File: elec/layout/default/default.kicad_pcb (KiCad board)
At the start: 4 copper layers, 76 x 146 mm, 103 parts, among them J1 ?, J2 ?, Q1 ?, SW1 ?, SW10 ?, SW11 ?, SW12 ?, SW13 ?, SW14 ?, SW15 ?, SW16 ?, SW17 ?, SW18 ?, SW19 ?, SW2 ?, SW20 ?, SW21 ?, SW22 ?, SW23 ?, SW24 ?, SW25 ?, SW26 ?, SW27 ?, SW28 ?, SW29 ?, SW3 ?, SW30 ?, SW31 ?, SW32 ?, SW33 ?, SW34 ?, SW35 ?, SW36 ?, SW37 ?, SW38 ?, SW39 ?, SW4 ?, SW40 ?, SW5 ?, SW6 ?, SW7 ?, SW8 ?, SW9 ?, U1 ?, U2 ?, U3 ?, U4 ?, U5 ?, U6 ?, U7 ?, U8 ?

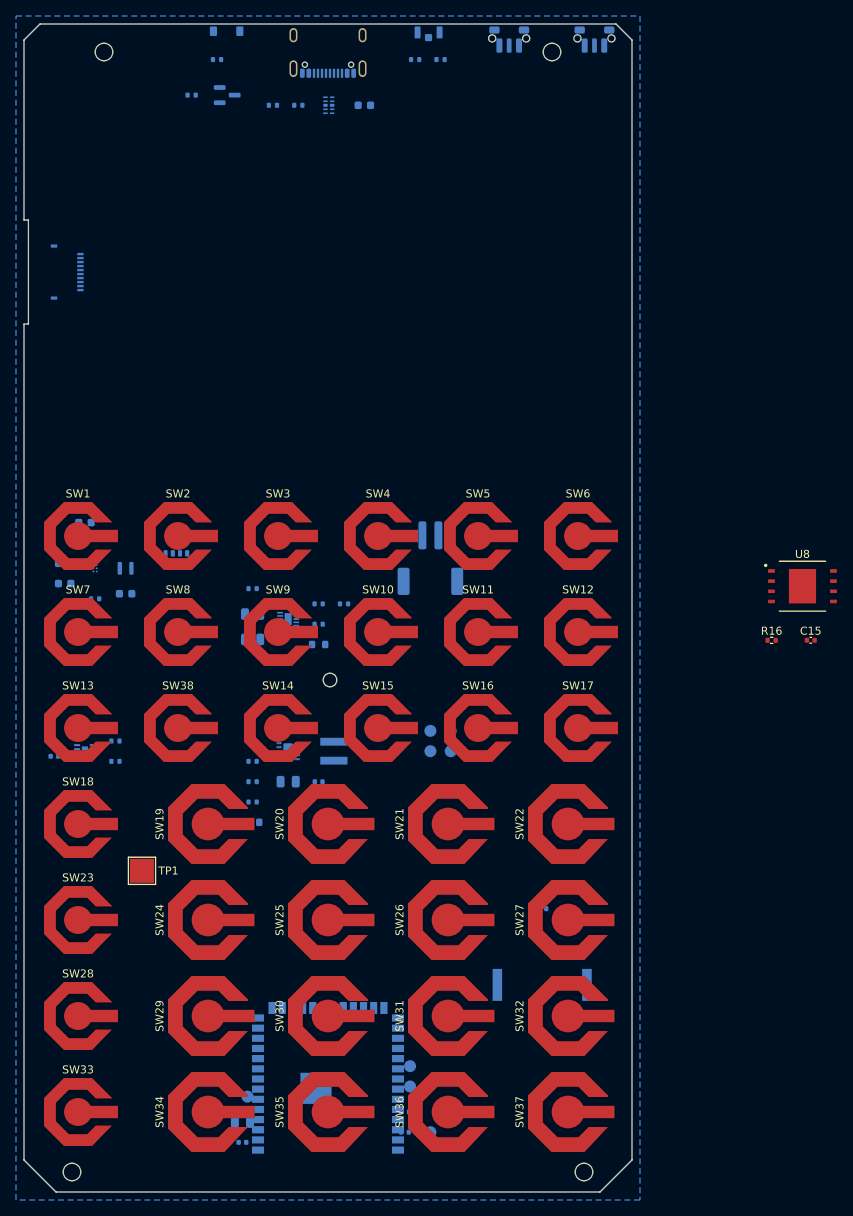
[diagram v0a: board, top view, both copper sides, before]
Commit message: mip: WROOM area and NAND placed, board fully rerouted at 146
104 nets, 0 failed; check_ends, check_pour, NPTH clean; antenna keepout
X 14..62 from Y 141.25 empty. fix_footprint_zones.py mirrors zones of
back-side footprints (U5's keepout; both Alps keepouts were on the wrong
side). C8/C9 share U5 pin 2's plane via. Bench pin map for the Waveshare
LCD-Driver board in docs/bench-lcd-driver-board.md.

Co-Authored-By: Claude Opus 5.5 (1M context) <noreply@anthropic.com>
Claude-Session: https://claude.ai/code/session_01Fsrot3PauY1JdFC7HgzJ33
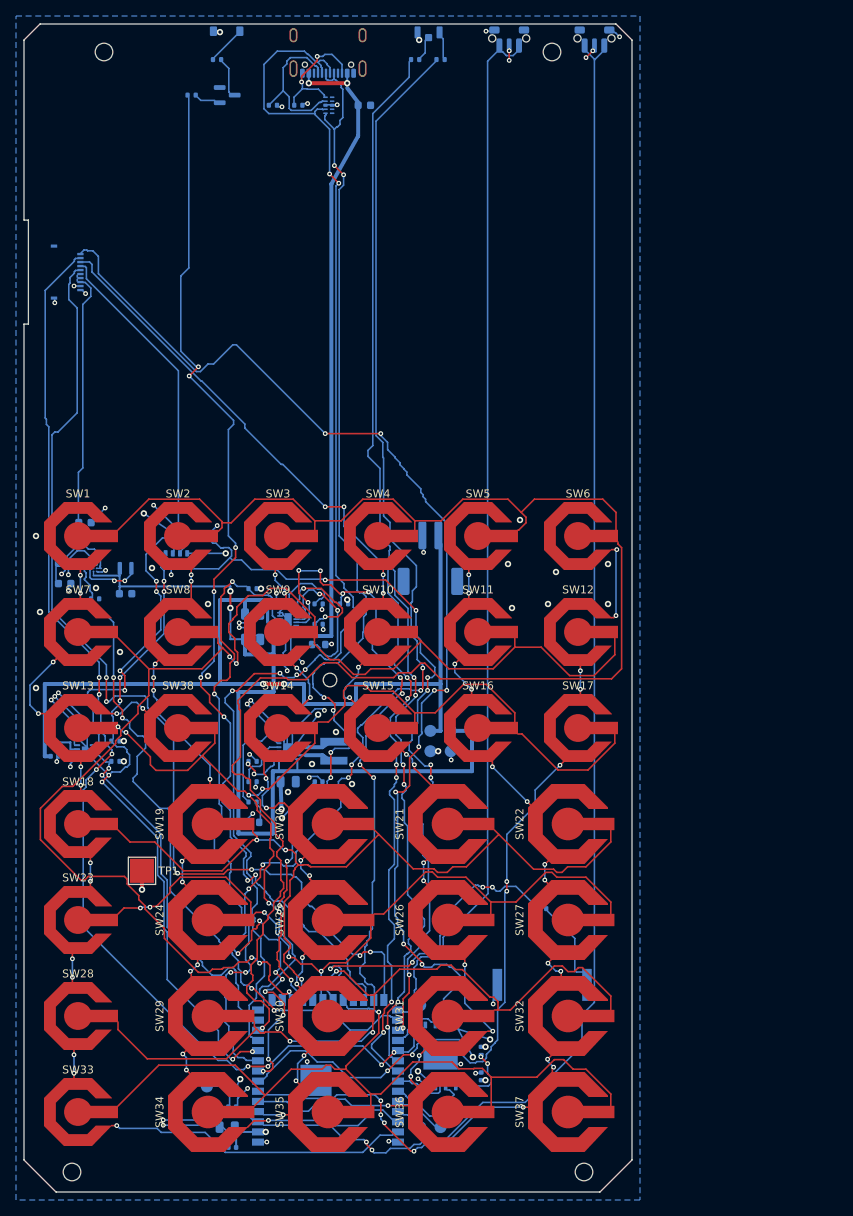
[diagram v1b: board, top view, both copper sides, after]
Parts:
- C15, R16, U8: moved to B.Cu
- moved U8 74.1 mm to (52.1, 129.0), turned to 90 degrees
- moved C15 68.3 mm to (57.1, 131.5), turned to 90 degrees
- moved R16 62.9 mm to (57.1, 128.4), turned to 90 degrees
- moved TP8 28.5 mm to (22.9, 132.8)
- moved TP9 24.4 mm to (49.5, 122.7)
- moved C7 21.8 mm to (26.0, 135.3)
- moved R13 21.8 mm to (26.0, 132.8)
- moved TP7 8.52 mm to (52.1, 137.9)
- moved TP6 5.24 mm to (49.5, 137.9)
- moved C8 2.01 mm to (25.4, 137.9), turned to 180 degrees
- moved C9 1.42 mm to (26.0, 140.4), turned to 180 degrees
- moved U5 1.00 mm to (38.0, 134.5)
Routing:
- net row0: track 0.00 -> 200.1 mm, vias 0 -> 1
- net en: track 0.00 -> 180.6 mm, vias 0 -> 2
- net row1: track 0.00 -> 164.0 mm, vias 0 -> 5
- net usb_dm: track 0.00 -> 157.1 mm, vias 0 -> 6
- net led_red: track 0.00 -> 151.9 mm, vias 0 -> 8
- net mip_sck: track 0.00 -> 145.0 mm, vias 0 -> 8
- net mip_mosi: track 0.00 -> 143.8 mm, vias 0 -> 8
- net usb_dp: track 0.00 -> 138.7 mm, vias 0 -> 8
- net led_green: track 0.00 -> 135.0 mm, vias 0 -> 6
- net ir_led: track 0.00 -> 132.2 mm, vias 0 -> 8
- net boot: track 0.00 -> 128.2 mm
- net mip_disp: track 0.00 -> 126.2 mm, vias 0 -> 6
- net gnd: track 0.00 -> 125.6 mm, vias 0 -> 72
- net mip_cs: track 0.00 -> 125.5 mm, vias 0 -> 8
- net row2: track 0.00 -> 117.7 mm, vias 0 -> 7
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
